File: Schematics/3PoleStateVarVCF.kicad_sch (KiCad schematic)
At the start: 158 parts, among them J54 Conn_01x04, J55 Conn_01x03, J56 Conn_01x04, J57 Conn_01x04, U238 PCF8574, U239 LM78L05, U242 AMS1117-3.3, U270 DG212C, U277 DG212C, U32 SSI2164, U33 TL072, U34 TL074, U35 TL074, U36 TL074, U37 TL072, U38 TL074, U39 SSI2164, U40 MCP4728, U41 TL072, U42 TL072, U43 TL072

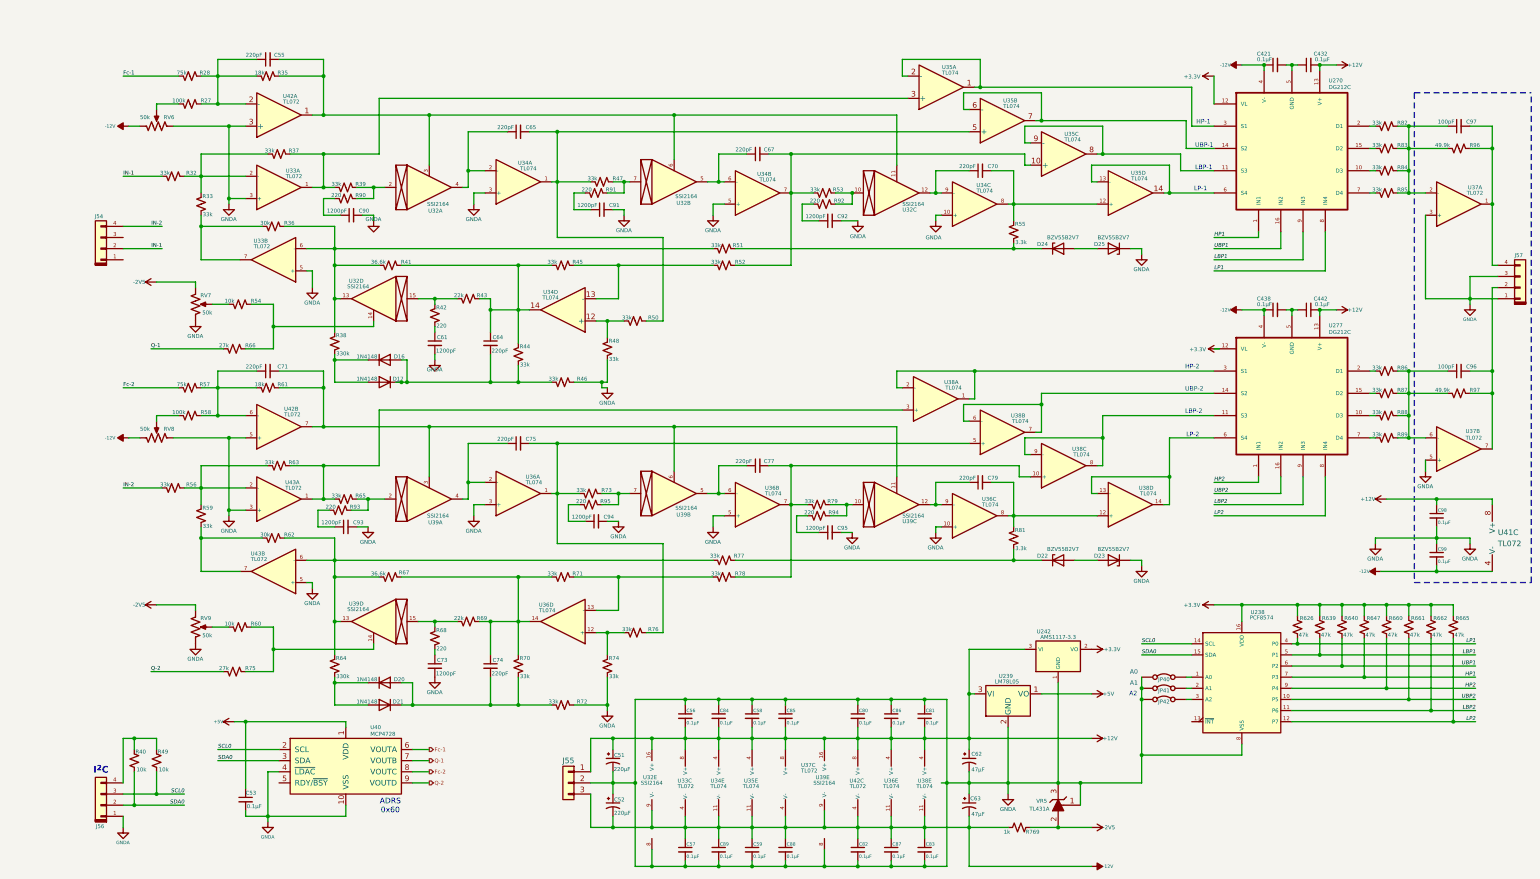
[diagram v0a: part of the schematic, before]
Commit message: Updated to more automation on the Launch Control XL.  Added pageing controls for filter page on display.  Prepped interface for adding filter controls.  Added Filter data to configureation saves.
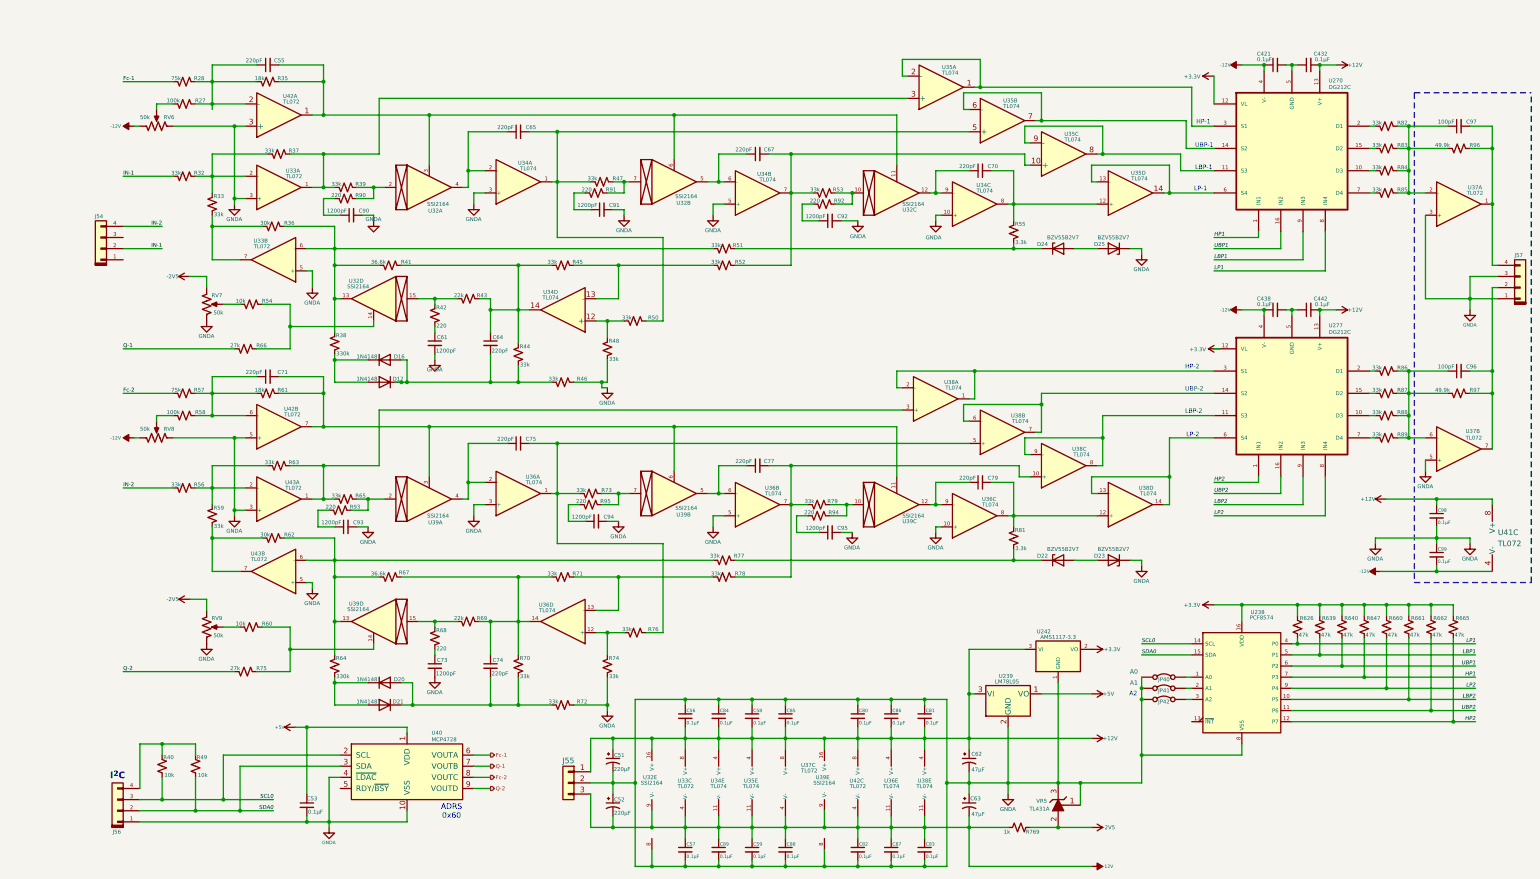
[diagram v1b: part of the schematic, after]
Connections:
- net HP2: now also R665.2, U238.12 (P7); no longer R660.2, U238.9 (P4)
- net LBP2: now also R661.2, U238.10 (P5); no longer R662.2, U238.11 (P6)
- net LP2: now also R660.2, U238.9 (P4); no longer R665.2, U238.12 (P7)
- net SCL0: now also R40.2; no longer R49.2
- net SDA0: now also R49.2; no longer R40.2
- net UBP2: now also R662.2, U238.11 (P6); no longer R661.2, U238.10 (P5)
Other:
- moved on the sheet: C53, C55, C71, J56, R27, R28, R32, R33, R35, R40, R49, R54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

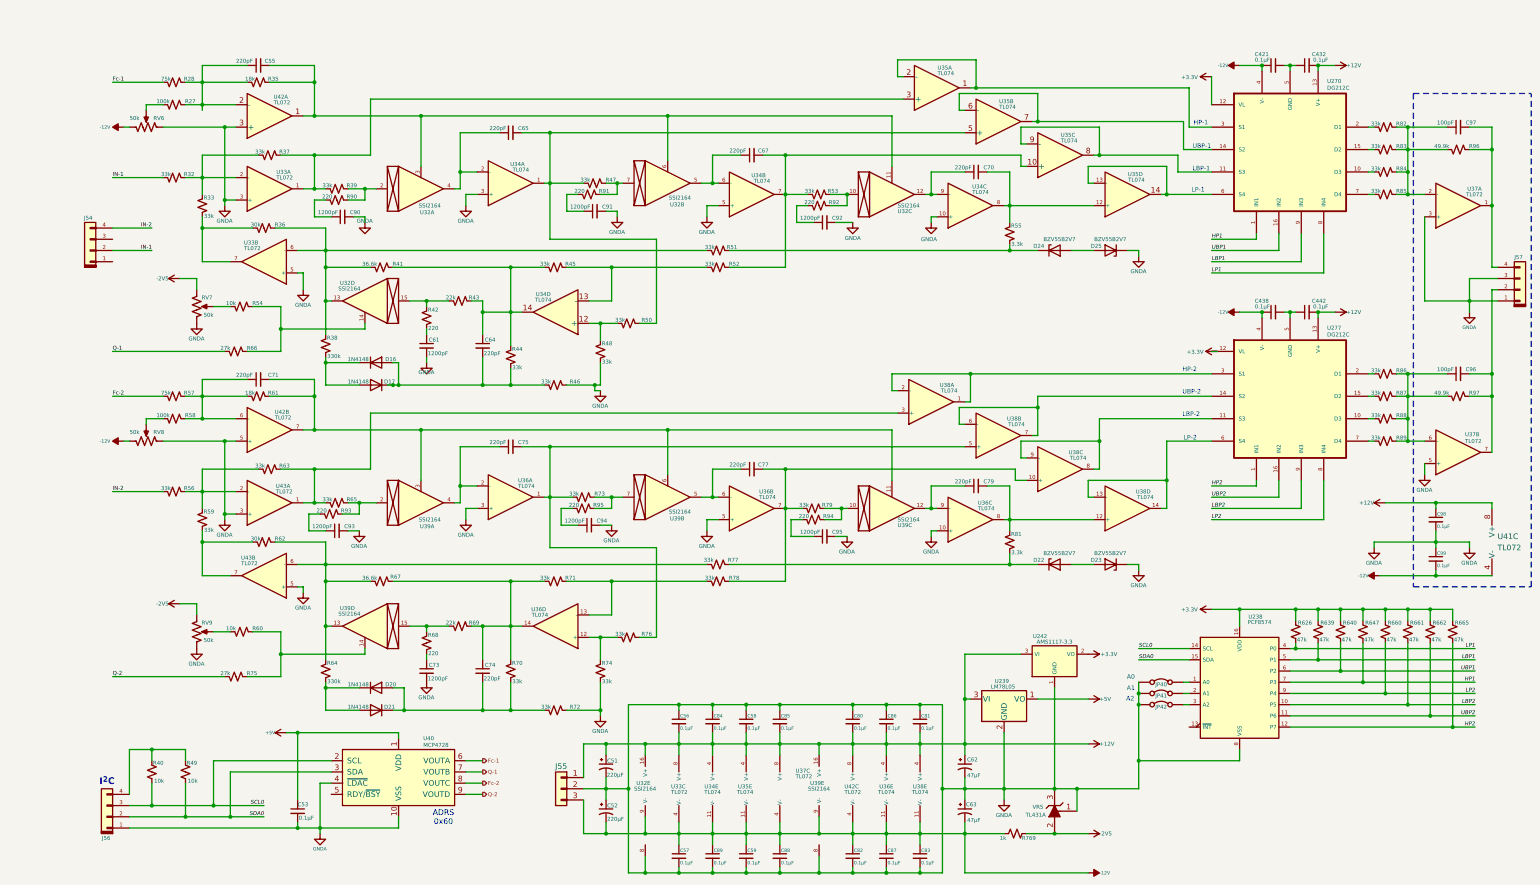
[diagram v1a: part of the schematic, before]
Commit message: Started changing some byte passing to int for more effiencency.  Completed configuration for the envelope generator to go in either direction and controls of start and end values.  Changed oscillator bypass to be controlled on the filter page and the first two input modes, fixed and envelope, are working.  Will need to add the modulator yet but will wait until 3 more filter boards are working.
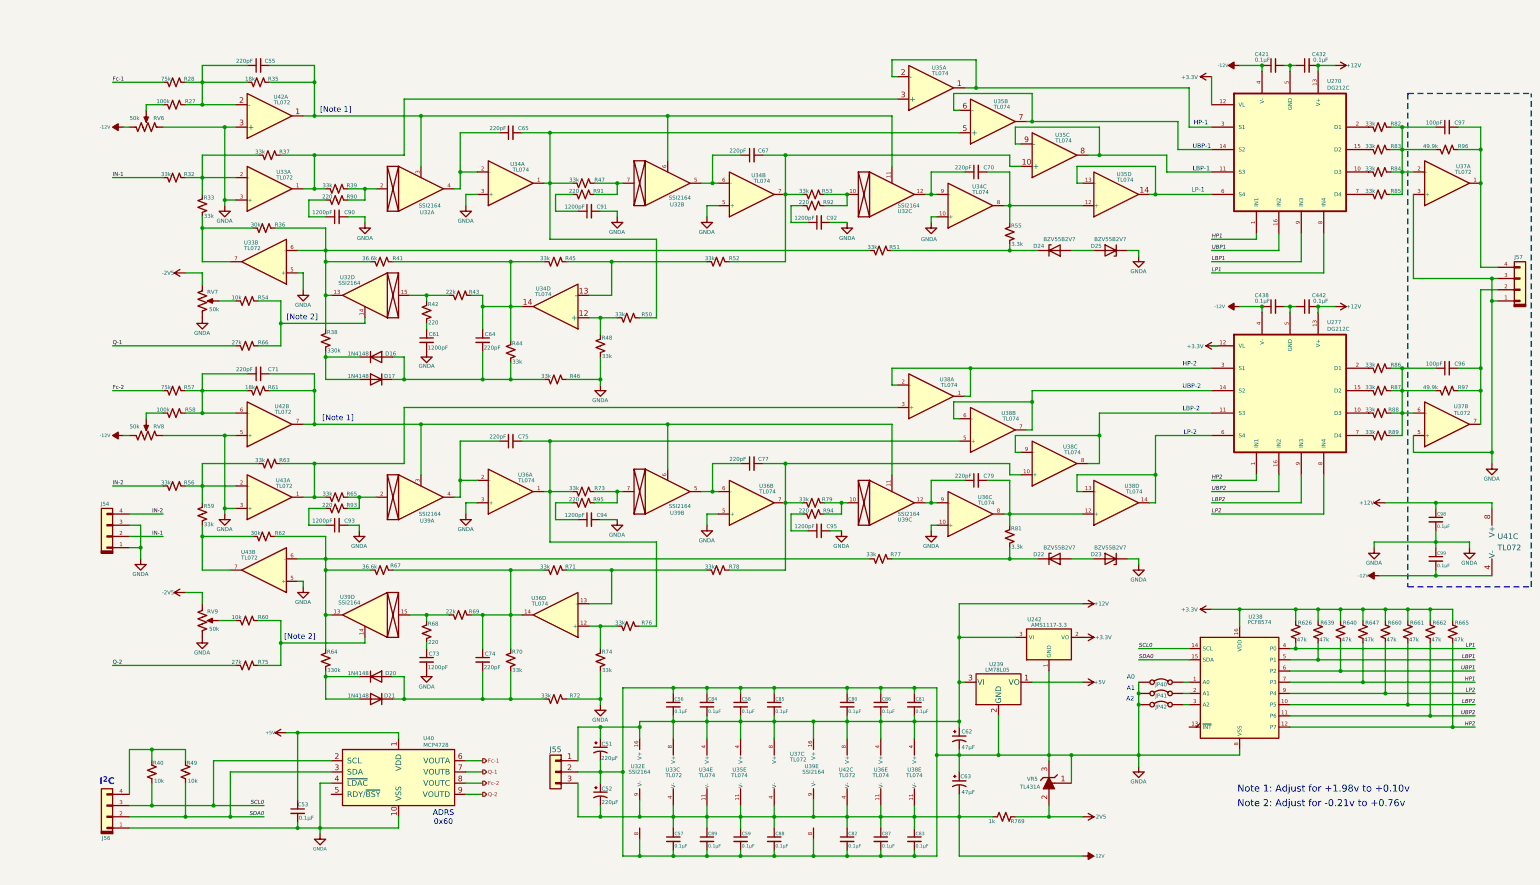
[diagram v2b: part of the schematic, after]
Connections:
- net GNDA: now also J54.1 (Pin_1), J54.3 (Pin_3)
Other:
- note added: "Note 1: Adjust for +1.98v to +0.10v"
- note added: "Note 2: Adjust for -0.21v to +0.76v"
- note added: "[Note 1]"
- note added: "[Note 2]"
- moved on the sheet: C438, C442, C51, C52, C56, C57, C58, C59, C61, C62, C63, C64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

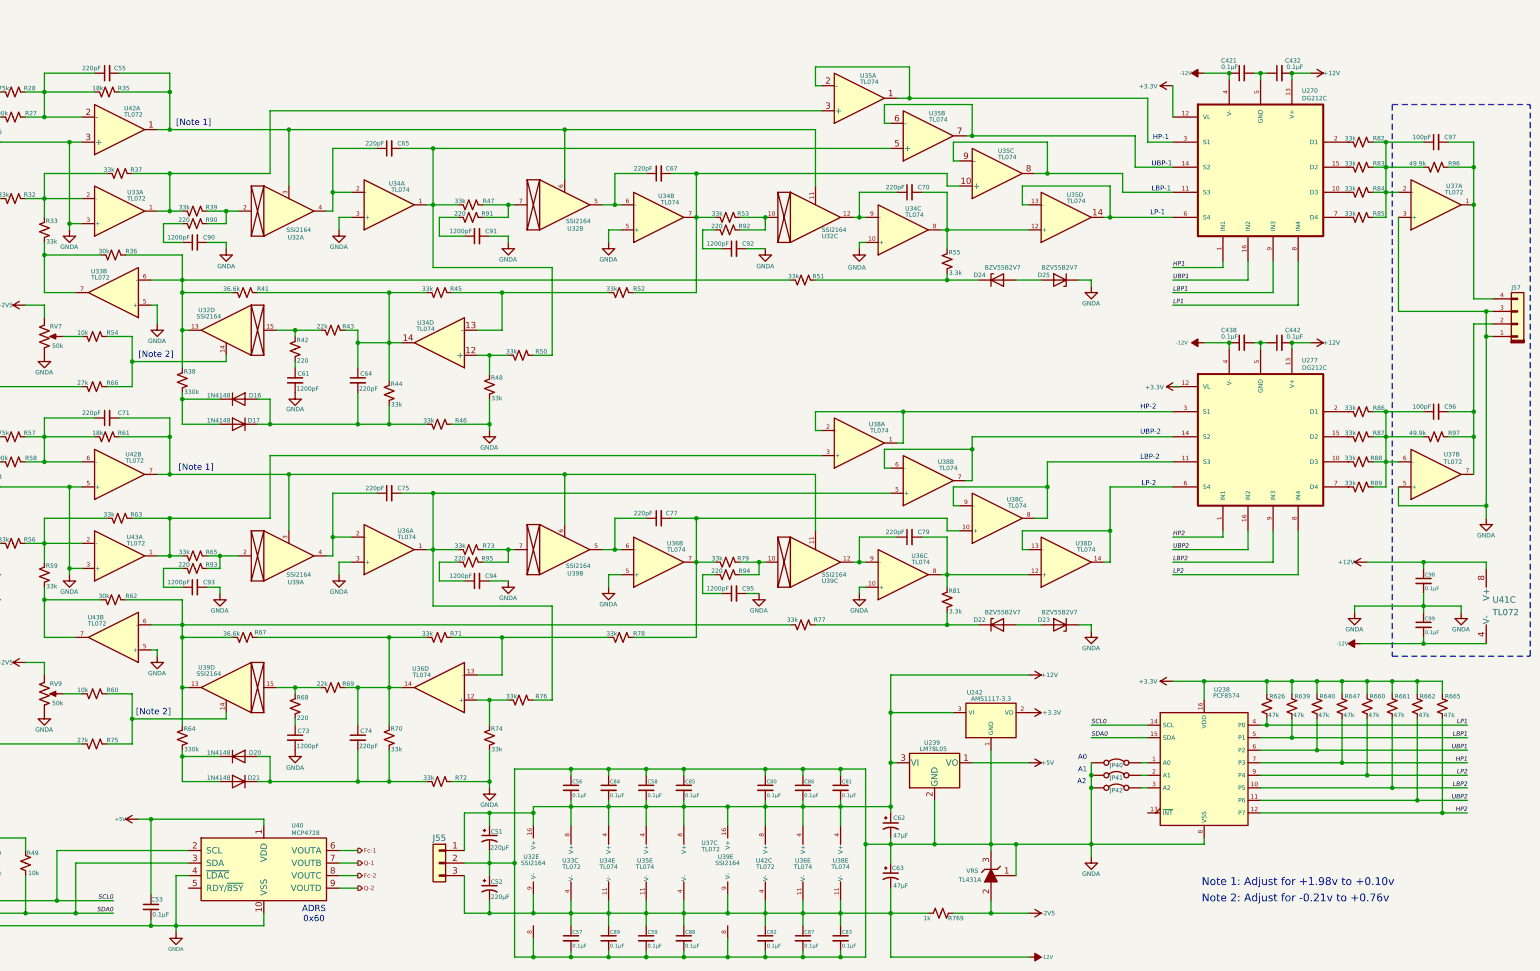
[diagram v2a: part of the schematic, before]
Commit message: - Added LED to power 3.3v - Enhanced tuning options to inlcude all filter outputs - Enhanced display for tuning control aditions. - Moved all tuning contrls to the G49.
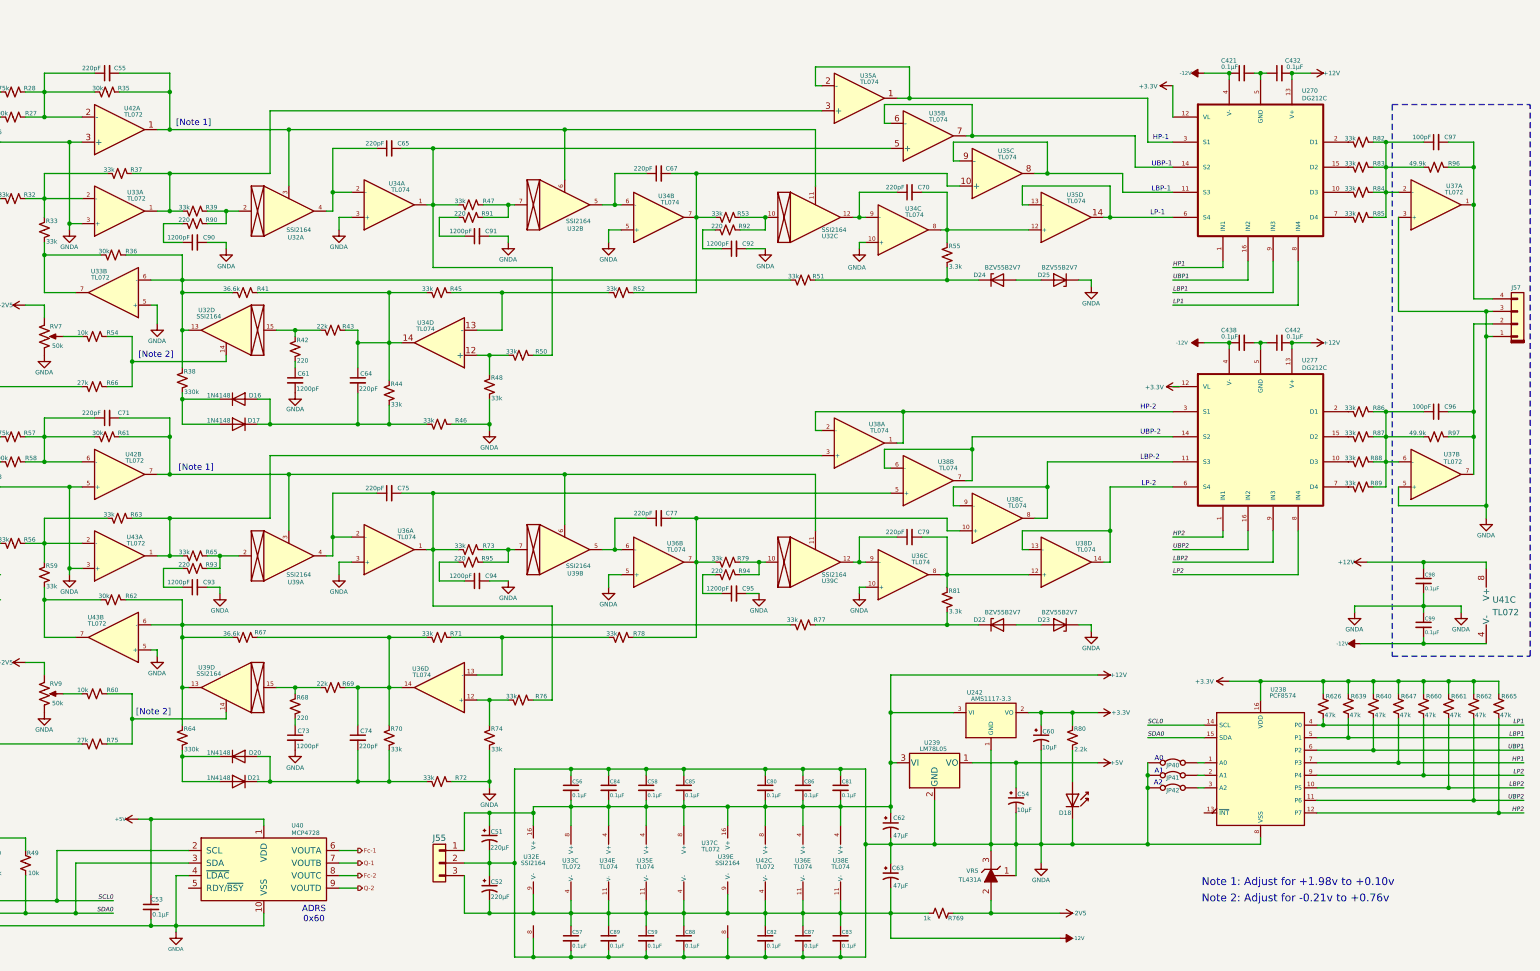
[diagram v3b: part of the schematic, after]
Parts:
- added C54, C60: 10µF, symbol Device:C_Polarized_Small_US
- added D18: SFH4356P, LED_THT:LED_D3.0mm_IRBlack, symbol LED:SFH4356P
- added R80: 2.2k, symbol Device:R_Small_US
- R35, R61: value 18k -> 30k
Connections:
- net +3.3V: now also C60.1, R80.1
- net +5V: now also C54.1
- net GNDA: now also C54.2, C60.2, D18.1 (K)
- new net: D18.2 (A), R80.2
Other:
- moved on the sheet: JP40, JP41, JP42, R55, R626, R639, R640, R647, R660, R661, R662, R665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

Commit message: New output mixer with VCAs
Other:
- note added: "ADRS 0x38"
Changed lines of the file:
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@@
 		)
 	)
+	(text "ADRS\n0x38"
+		(exclude_from_sim no)
+		(at 294.894 172.72 0)
+		(effects
+			(font
+				(size 1.27 1.27)
+			)
+		)
+	)
 	(text "Note 2: Adjust for -0.21v to +0.76v"
 		(exclude_from_sim no)
@@
 		(fields_autoplaced yes)
 		(property "Reference" "U41"
-			(at 335.28 124.4599 0)
+			(at 338.328 122.174 0)
 			(effects
 				(font
-					(size 1.27 1.27)
+					(size 0.889 0.889)
 				)
 				(justify left)
@@
 		)
 		(property "Value" "TL072"
-			(at 335.28 126.9999 0)
+			(at 338.328 123.444 0)
 			(effects
 				(font
-					(size 1.27 1.27)
+					(size 0.889 0.889)
 				)
 				(justify left)
@@
 					(reference "U41")
 					(unit 3)
+				)
+				(path "/718f017d-28fe-4e29-b548-40db8e21cec7/92fe7bea-64b6-40b3-8e51-c7dbcedff8cc/e229fcb1-b6f4-4b19-b740-d1e1a6c9a14c"
+					(reference "U41")
+					(unit 3)

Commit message: Updated 3 state filters to have more trimming settings.  Tweaks to fix initial envelope settings.
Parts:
- added R29, R30: 45k, symbol Device:R_Small_US
- added RV10, RV11: 50k, symbol Device:R_Potentiometer_US
- added RV12, RV13: 500k, symbol Device:R_Potentiometer_US
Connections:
- net Fc-1: now also RV10. (2)
- net Fc-2: now also RV11. (2)
- net at C97.1, R82.1, R83.1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: now also RV12. (2)
- net at C96.2, J57.2 (Pin_2), R97.1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: now also RV13. (2)
- net at C97.2, J57.4 (Pin_4), R96.1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: now also RV12. (2)
- net at C55.1, R27.1, R28.1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: now also R29.1
- net at C96.1, R86.1, R87.1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: now also RV13. (2)
- net at C71.1, R57.1, R58.1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: now also R30.1
- new net: R29.2, RV10. (2)
- new net: R30.2, RV11. (2)
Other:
- note added: "Board #1"
- moved on the sheet: C55, C71, C96, C97, R27, R28, R35, R57, R58, R61, R96, R97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
